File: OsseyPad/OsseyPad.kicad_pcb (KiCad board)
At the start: 2 copper layers, 152.4 x 142.9 mm, 66 parts

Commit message: Updated the pcb.
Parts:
- removed the D31 at (271.5, 183.4)
- removed D5: 1N4148W, Diode_SMD:D_SOD-123
- added C1: 0.1uF, Capacitor_SMD:C_0603_1608Metric, B.Cu at (182.0, 101.0)
- added C10: 100n, Capacitor_SMD:C_0603_1608Metric, B.Cu at (264.5, 79.5)
- added C2: 0.1uF, Capacitor_SMD:C_0603_1608Metric, B.Cu at (168.0, 100.0)
- added C3: 0.1uF, Capacitor_SMD:C_0603_1608Metric, B.Cu at (177.5, 94.0)
- added C4: 0.1uF, Capacitor_SMD:C_0603_1608Metric, B.Cu at (174.8, 106.0)
- added C5: 10uF, Capacitor_SMD:C_0603_1608Metric, B.Cu at (177.8, 106.3)
- added C6: 15pF, Capacitor_SMD:C_0603_1608Metric, B.Cu at (171.9, 92.5)
- added C7: 15pF, Capacitor_SMD:C_0603_1608Metric, B.Cu at (167.8, 96.6)
- added C8: 1uF, Capacitor_SMD:C_0603_1608Metric, B.Cu at (169.5, 103.5)
- added C9: 100n, Capacitor_SMD:C_0603_1608Metric, B.Cu at (264.5, 92.0)
- added D32: 1N4148W, Diode_SMD:D_SOD-123, B.Cu at (269.1, 183.4)
- added D6: 1N4148W, Diode_SMD:D_SOD-123, B.Cu at (169.1, 109.5)
- added F1: 500mA, Fuse:Fuse_0603_1608Metric, B.Cu at (162.9, 80.9)
- added FB1: 50 @ 100 MHz, Inductor_SMD:L_0805_2012Metric, B.Cu at (161.6, 82.7)
- added J1: USB_C_Receptacle_USB2.0, josh-connectors:USB_C_U262-161N-4BVC11, B.Cu at (177.3, 70.0)
- added R1: 10k, Resistor_SMD:R_0603_1608Metric, B.Cu at (168.0, 101.9)
- added R10: 5K1, Resistor_SMD:R_0603_1608Metric, B.Cu at (166.4, 80.9)
- added R11: 5K1, Resistor_SMD:R_0603_1608Metric, B.Cu at (167.8, 88.6)
- added R2: 22, Resistor_SMD:R_0603_1608Metric, B.Cu at (163.3, 89.2)
- added R3: 22, Resistor_SMD:R_0603_1608Metric, B.Cu at (161.6, 87.5)
- added R4: 10k, Resistor_SMD:R_0603_1608Metric, B.Cu at (183.5, 99.0)
- added R5: 10K, Resistor_SMD:R_0603_1608Metric, B.Cu at (268.0, 79.5)
- added R6: 10K, Resistor_SMD:R_0603_1608Metric, B.Cu at (268.0, 92.0)
- added R7: 10K, Resistor_SMD:R_0603_1608Metric, B.Cu at (266.2, 79.5)
- added R8: 10K, Resistor_SMD:R_0603_1608Metric, B.Cu at (266.2, 92.0)
- added R9: 10K, Resistor_SMD:R_0603_1608Metric, B.Cu at (285.5, 80.2)
- added SW1: Rotary_Encoder_Switch, Rotary_Encoder:RotaryEncoder_Alps_EC11E-Switch_Vertical_H20mm_CircularMountingHoles, F.Cu at (268.7, 83.2)
- added SW2: SW_Push, Button_Switch_THT:SW_PUSH_6mm_H8mm, B.Cu at (145.2, 82.0)
- added U1: USBLC6-2SC6, Package_TO_SOT_SMD:SOT-23-6, B.Cu at (164.9, 85.9)
- added U2: ATmega32U4-MU, Package_DFN_QFN:QFN-44-1EP_7x7mm_P0.5mm_EP5.2x5.2mm, B.Cu at (176.0, 99.9)
- added Y1: 16MHz, Crystal:Crystal_SMD_3225-4Pin_3.2x2.5mm, B.Cu at (169.8, 94.5)
- moved D16 3.11 mm to (269.1, 126.2), turned to 270 degrees
- moved D11 2.38 mm to (269.1, 107.2), turned to 270 degrees
- moved D22 2.38 mm to (269.1, 145.3), turned to 270 degrees
- moved D27 2.38 mm to (269.1, 164.3), turned to 270 degrees
- renumbered D9 to D10, D10 to D11, D11 to D12, D12 to D13, D13 to D14, D14 to D15, D15 to D16, D16 to D17, D17 to D18, D18 to D19, D19 to D20, D20 to D21, D21 to D22, D22 to D23, D23 to D24, D24 to D25, D25 to D26, D26 to D27, D27 to D28, D28 to D29, D29 to D30, D30 to D31, D6 to D7, D7 to D8, D8 to D9
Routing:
- net ROW5: track 0.00 -> 325.0 mm
- net COL4: track 0.00 -> 302.0 mm, vias 0 -> 1
- net ROW4: track 0.00 -> 296.4 mm
- net COL5: track 0.00 -> 284.7 mm, vias 0 -> 1
- net ROW3: track 0.00 -> 283.6 mm
- net COL3: track 0.00 -> 274.5 mm, vias 0 -> 1
- net COL2: track 0.00 -> 271.6 mm, vias 0 -> 1
- net ROW2: track 0.00 -> 255.9 mm
- net COL1: track 0.00 -> 250.5 mm, vias 0 -> 1
- net ROW1: track 0.00 -> 236.3 mm, vias 0 -> 2
- net COL0: track 0.00 -> 200.2 mm, vias 0 -> 1
- net ENC_1_SW: track 0.00 -> 135.5 mm
- net ENC_1_B: track 0.00 -> 121.5 mm
- net ENC_1_A: track 0.00 -> 109.3 mm
- net ROW0: track 0.00 -> 93.4 mm
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- added copper zone on In2.Cu, net +5V
- added copper zone on In1.Cu, net GND
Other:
- copper layers 2 -> 4
- net class Default: clearance 0.2 -> 0.19
- rule trace_clearance: 0.2 -> 0.19

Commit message: Updatet the pcb and added first versio off the firmware.
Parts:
- removed R9: 10K, Resistor_SMD:R_0603_1608Metric
- added D5: 1N4148W, Diode_SMD:D_SOD-123, B.Cu at (153.5, 50.0)
- added G***: LOGO, OsseyPad:HelloToHorse, B.Cu at (139.3, 154.5)
- moved C1 130.5 mm to (59.5, 56.0)
- moved C10 130.5 mm to (142.0, 34.5)
- moved C2 130.5 mm to (45.5, 55.0)
- moved C3 130.5 mm to (55.0, 49.0)
- moved C4 130.5 mm to (52.2, 61.0)
- moved C5 130.5 mm to (55.3, 61.4)
- moved C6 130.5 mm to (49.4, 47.5)
- moved C7 130.5 mm to (45.3, 51.6)
- moved C8 130.5 mm to (47.0, 58.5)
- moved C9 130.5 mm to (142.0, 47.0)
- moved D1 130.5 mm to (75.1, 33.6)
- moved D10 130.5 mm to (132.3, 62.2)
- moved D11 130.5 mm to (146.6, 62.2)
- moved D12 130.5 mm to (46.6, 81.2)
- moved D13 130.5 mm to (75.1, 81.2)
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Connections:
- R2 pad 1: D+ -> D_Filt_+
- R3 pad 1: D- -> D_Filt_-
- SW1 pad S1: +5V -> COL5
- SW1 pad S2: ENC_1_SW -> Net-(D5-Pad2)
- U2 pad 20: ENC_1_SW -> Net-(U2-Pad20)
- U2 pad 3: D- -> D_Filt_-
- U2 pad 4: D+ -> D_Filt_+
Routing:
- net ENC_1_SW: track 135.5 -> 0.00 mm
- net D-: track 83.1 -> 1.68 mm
- net D+: track 81.6 -> 1.68 mm
- net D_Filt_-: track 0.00 -> 42.1 mm
- net D_Filt_+: track 0.00 -> 40.5 mm
- net ROW0: track 93.4 -> 128.1 mm
- net COL5: track 284.7 -> 316.9 mm
- net Net-(D5-Pad2): track 0.00 -> 19.5 mm
- net COL0: track 200.2 -> 210.7 mm
- net Net-(D22-Pad2): track 0.00 -> 9.86 mm
- net GND: track 64.0 -> 73.0 mm, vias 23 -> 29
- net VCC: track 40.9 -> 48.2 mm, vias 0 -> 2
- net COL4: track 302.0 -> 299.0 mm
- net COL2: track 271.6 -> 268.8 mm
- net COL1: track 250.5 -> 247.6 mm
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- added copper zone on B.Cu, net (none)
- added copper zone on F.Cu, net (none)
- added copper zone on In1.Cu_+5V, net +5V
- added copper zone on In2.Cu_GND, net GND
- removed copper zone on In2.Cu, net +5V
- removed copper zone on In1.Cu, net GND
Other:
- board text added: "OsseyPad Rev. 1.0"

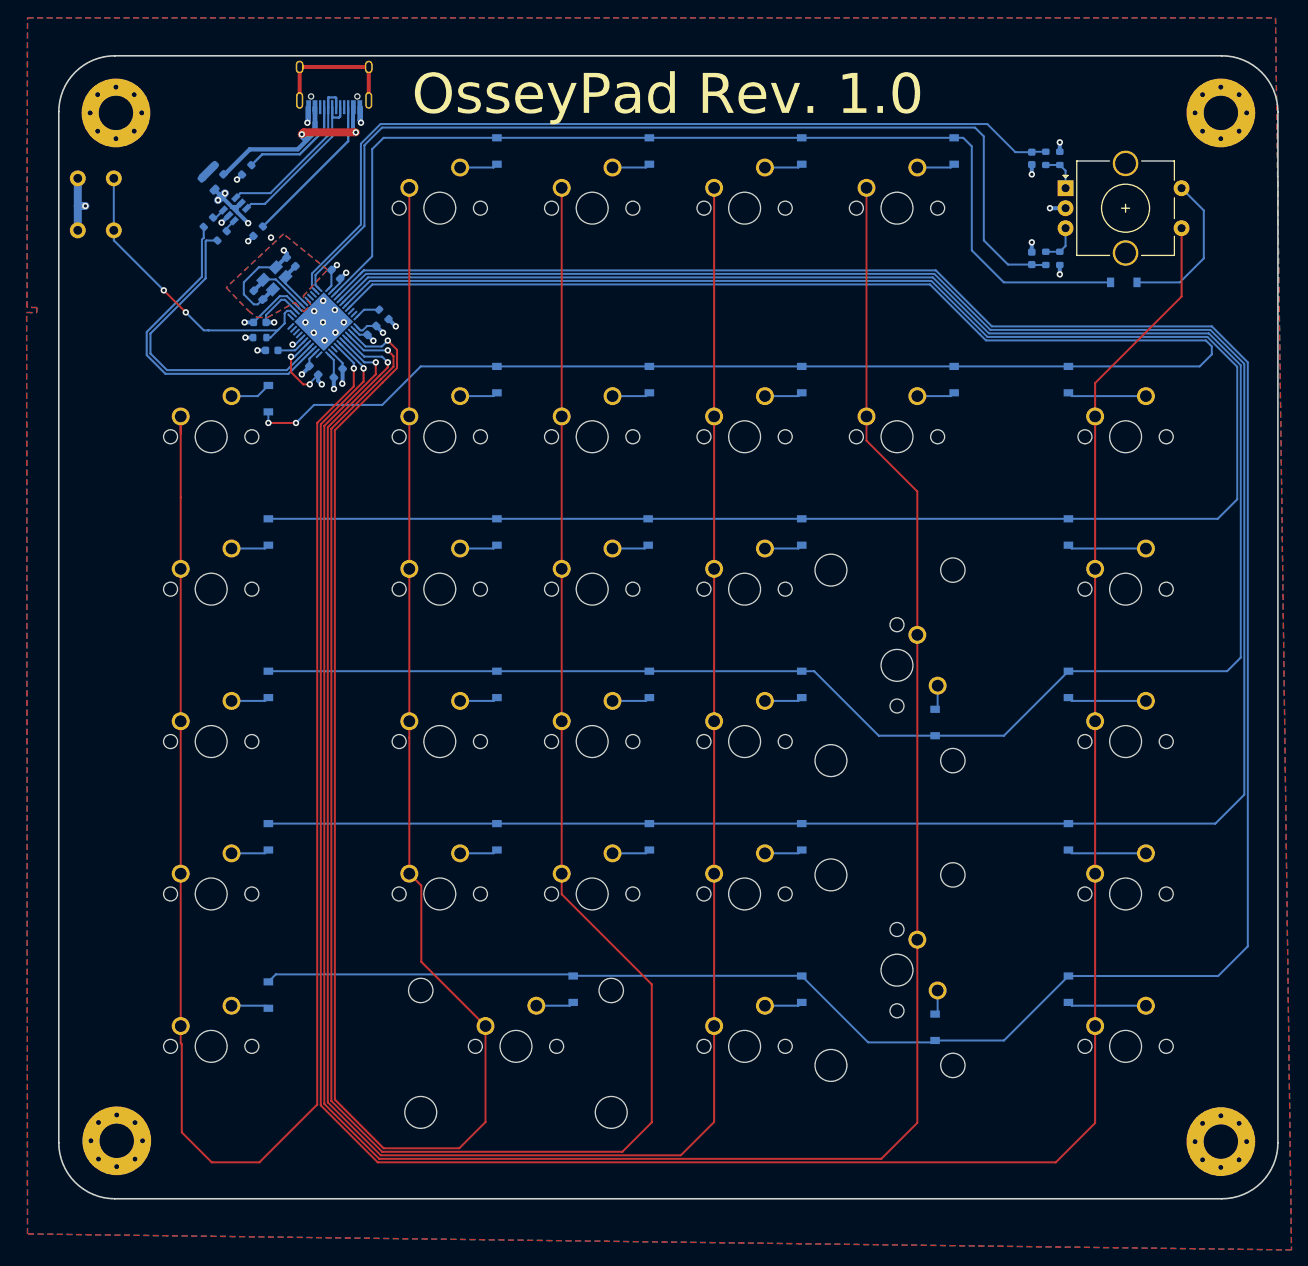
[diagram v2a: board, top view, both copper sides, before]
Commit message: Updatet the pcb and added models for the case.
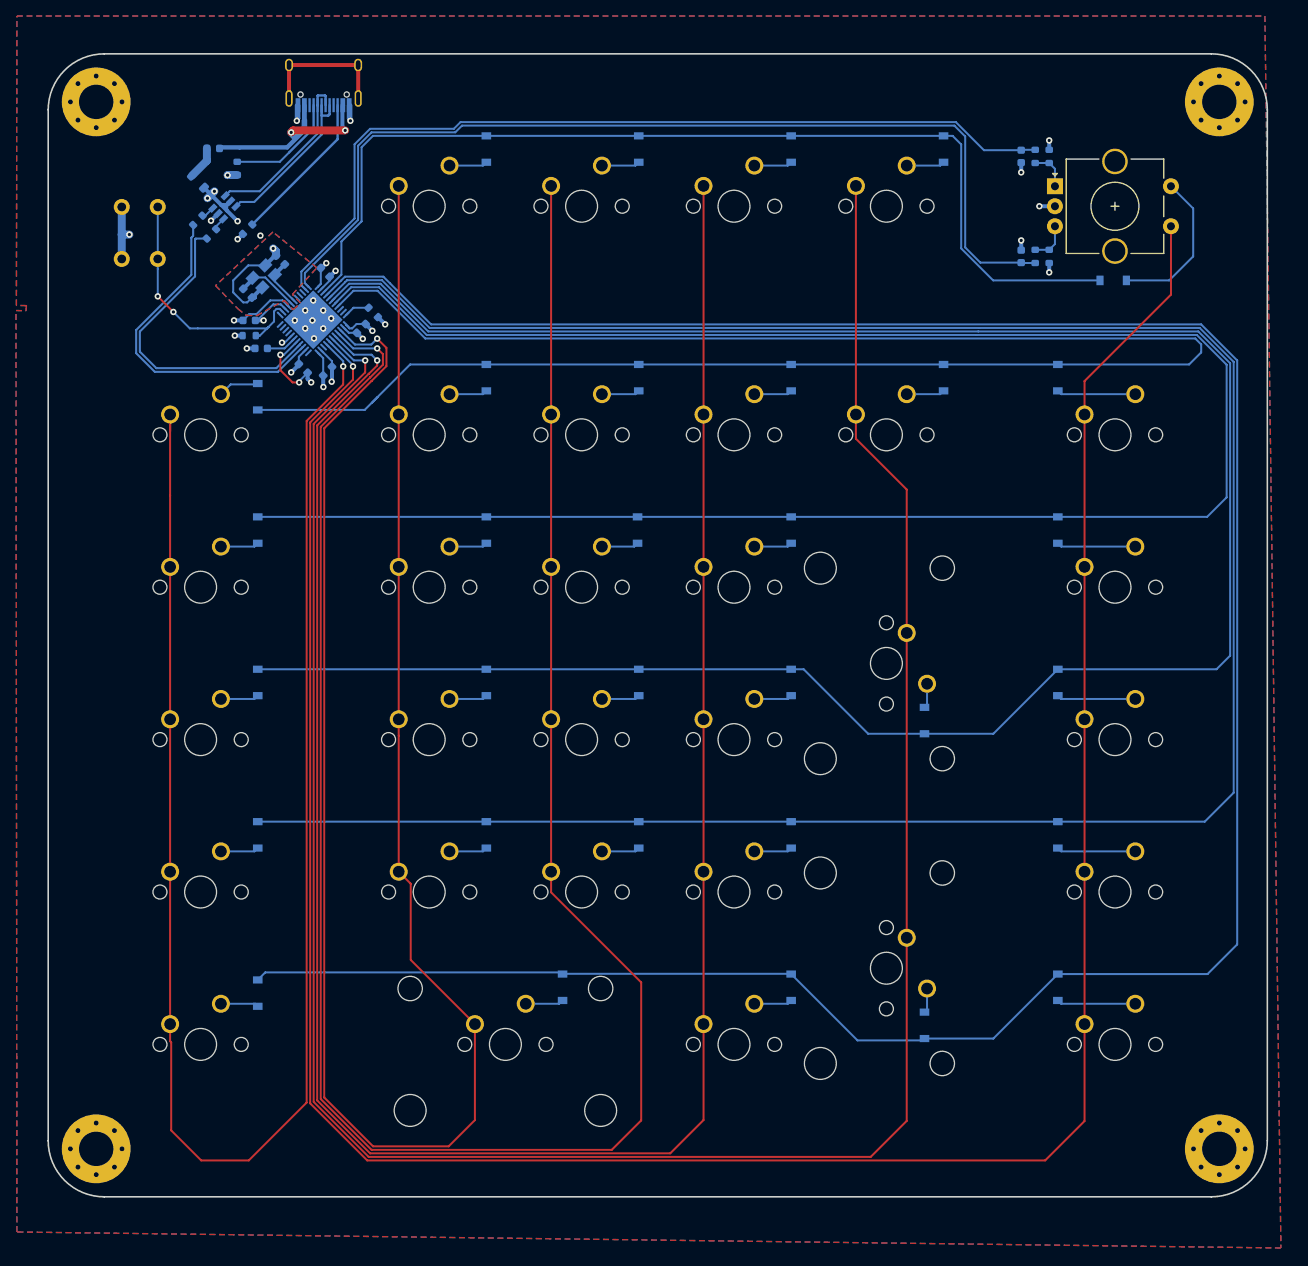
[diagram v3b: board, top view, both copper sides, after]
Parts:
- moved SW2 6.55 mm to (28.2, 40.6)
- moved H1 2.83 mm to (25.1, 27.4)
- moved F1 2.77 mm to (39.7, 33.3), turned to 180 degrees
- moved H3 2.76 mm to (25.1, 158.3)
- moved H2 1.39 mm to (165.4, 27.4)
- moved D27 1.35 mm to (145.3, 119.1)
- moved G*** 1.35 mm to (137.9, 154.2)
- moved D11 1.35 mm to (145.3, 61.9)
- moved D16 1.35 mm to (145.3, 81.0)
- moved D22 1.35 mm to (145.3, 100.0)
- moved D32 1.35 mm to (145.3, 138.1)
- moved D23 1.35 mm to (45.2, 119.1)
- moved D24 1.35 mm to (73.8, 119.1)
- moved D26 1.35 mm to (111.9, 119.1)
- moved D28 1.35 mm to (45.2, 138.8)
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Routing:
- net RESET: track 38.9 -> 32.5 mm
- net VCC: track 48.2 -> 44.1 mm
- net Net-(F1-Pad2): track 2.16 -> 4.18 mm
- net ROW1: track 236.3 -> 234.5 mm, vias 2 -> 0
- net ROW5: track 325.0 -> 323.5 mm
- net +5V: track 38.5 -> 37.3 mm
- net ROW4: track 296.4 -> 295.6 mm
- net ROW3: track 283.6 -> 282.8 mm
- net ROW2: track 255.9 -> 255.0 mm

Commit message: PCB Update.
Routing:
- net GND: track 72.7 -> 65.2 mm, vias 29 -> 28
- net COL1: track 247.6 -> 249.6 mm
- net COL2: track 268.8 -> 270.4 mm
- net COL5: track 316.9 -> 318.5 mm
- net COL3: track 271.7 -> 273.3 mm
- net COL4: track 299.0 -> 300.2 mm
